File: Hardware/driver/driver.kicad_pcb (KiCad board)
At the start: 4 copper layers, 128.1 x 184.5 mm, 191 parts, among them J201 Conn_02x10_Odd_Even, J302 Würth 74651194R, J303 Würth 74651194R, J401 TBP02R2W-381-03BE, J402 Conn_01x02_Male, J501 Conn_Coaxial, J601 Screw_Terminal_01x02, K601 EC2-5TNU, M201 Fan_4pin, Q201 MMBT3904, Q202 PN2222A, Q301 IXTH80N075L2, Q302 IXTH80N075L2, Q601 MMBT3904, Q602 MMBT3904, U101 ICL7660, U102 DS2482-100, U103 PI4IOE5V9536, U201 AT24CS32-SSHM, U202 MIC5366-3.3YC5, U203 ADUM1250, U204 MCP1804x-C002xMB, U205 FODM217B, U206 EMC2101-R, U207 MCP1703AT-5002E/DB, U301 MCP3421A2T-ECH, U302 ADA4522-2, U303 DAC60501Z, U304 LM431SC, U305 MCP3421A3T-ECH, U306 ADA4522-2, U307 DAC60501Z, U308 LM431SC, U309 DS18B20, U310 DS18B20, U501 74LVC1G17, U502 FODM217B, U601 MCP3421A1T-ECH, U602 OPA277

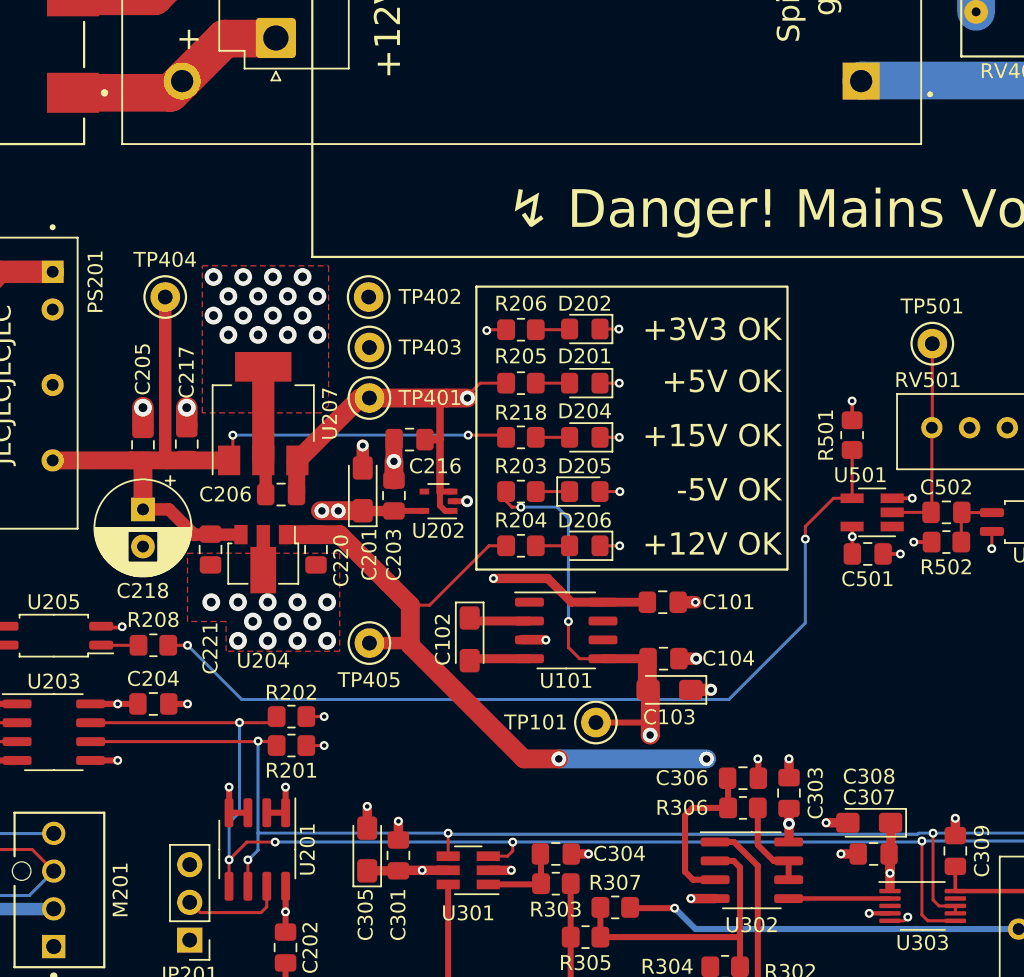
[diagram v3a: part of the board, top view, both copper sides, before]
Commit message: Fixed I2C bus reversal on driver
- Fixed an issue where SCL and SDA for the I2C bus were swapped beyond
  the interface sheet, meaning only the EEPROM is accessible over the
  bus. (This can probably be bodged relatively simply on a rev1 board on
  the bottom where the I2C bus runs)

- Manufacturability tweaks for TDK choke
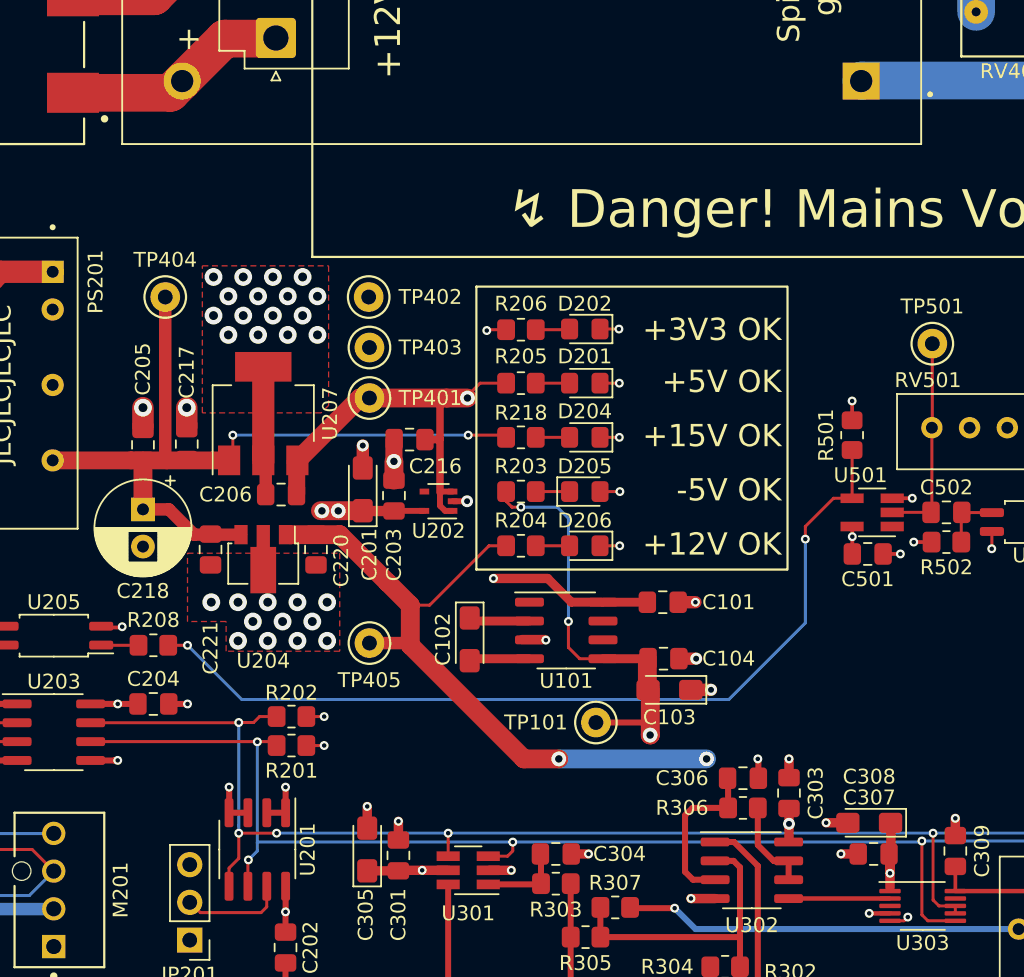
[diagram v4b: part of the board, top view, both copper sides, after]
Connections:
- R201 pad 1: /I2C_SDA -> /I2C_SCL
- R202 pad 1: /I2C_SCL -> /I2C_SDA
- U201 pad 5: /I2C_SCL -> /I2C_SDA
- U201 pad 6: /I2C_SDA -> /I2C_SCL
- U203 pad 6: /I2C_SDA -> /I2C_SCL
- U203 pad 7: /I2C_SCL -> /I2C_SDA
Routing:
- net /I2C_SCL: track 274.8 -> 271.7 mm, vias 10 -> 9
- net /I2C_SDA: track 266.2 -> 268.8 mm, vias 13 -> 14

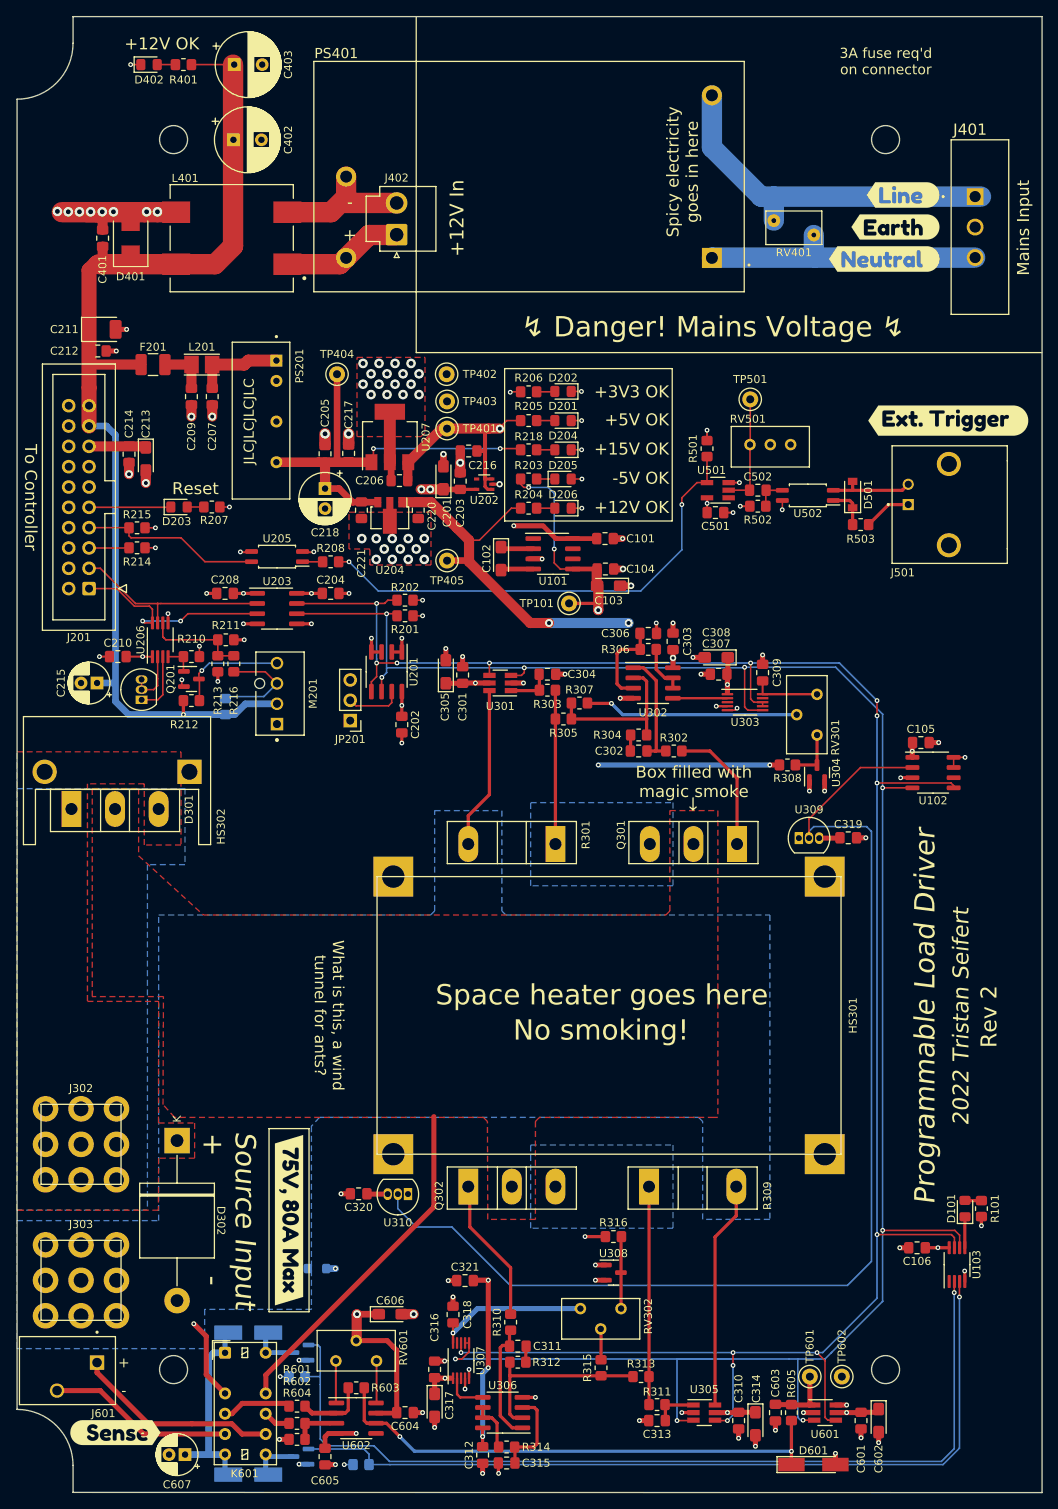
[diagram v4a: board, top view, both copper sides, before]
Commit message: Final bits of tweaks for rev2 analog board
- Fixed footprint of MMBT3904 transistors on driver and controller
  boards (it is SOT-323, not SC-70)

- A few more minor modifications to the layout of the analog driver
  board for rev2
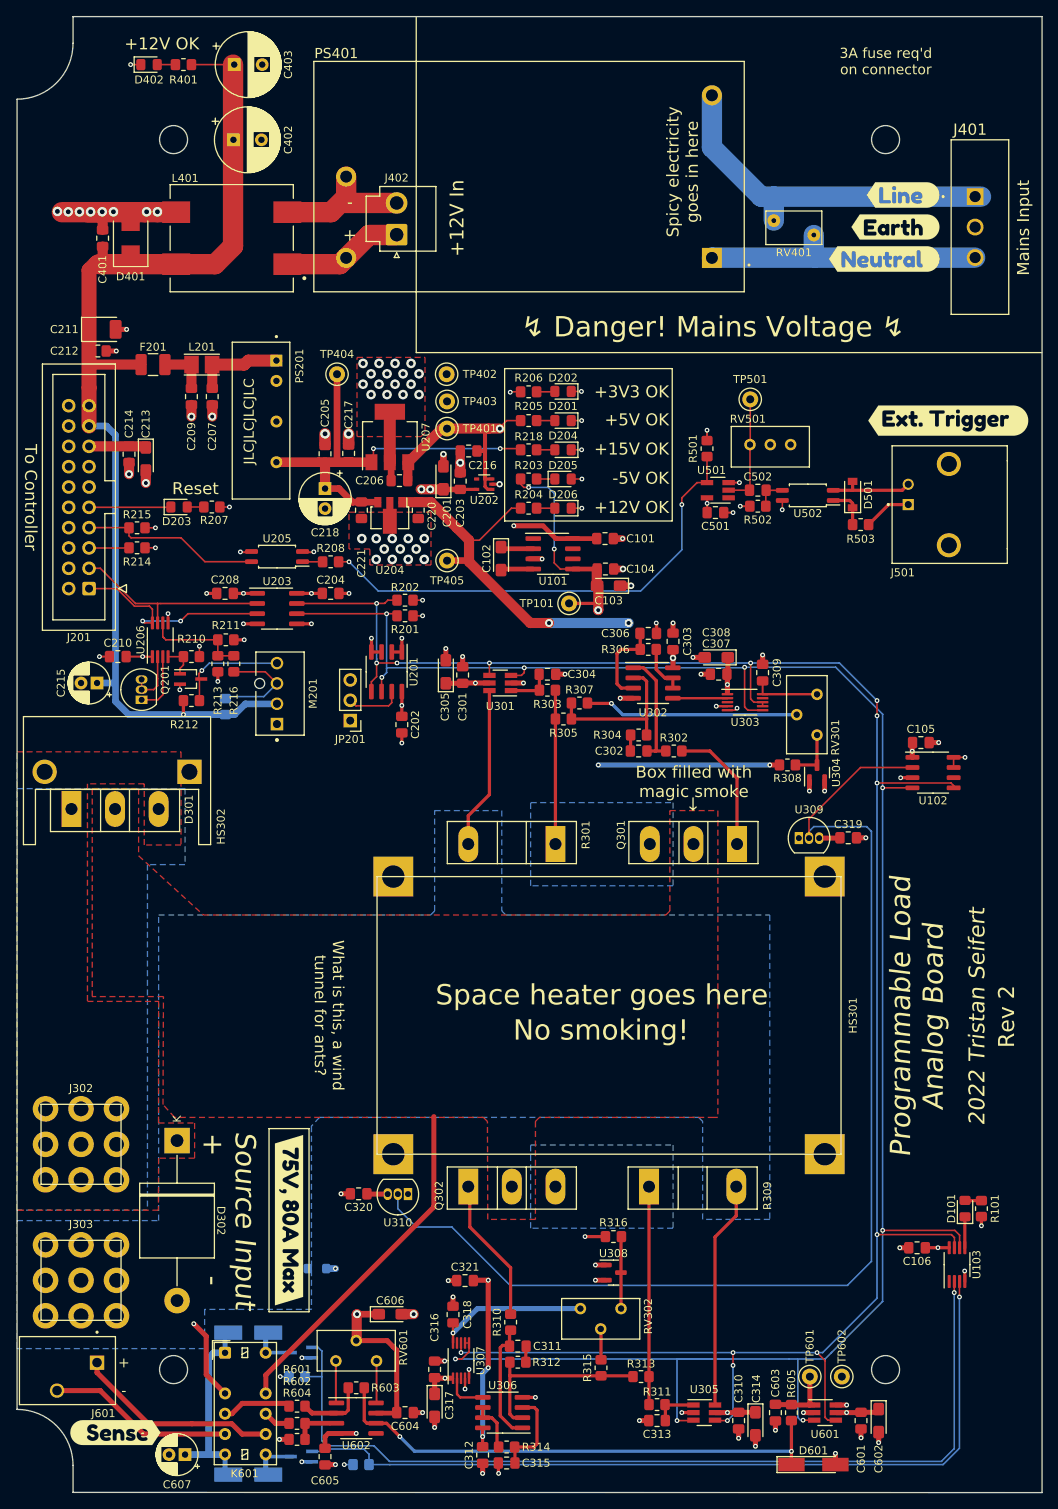
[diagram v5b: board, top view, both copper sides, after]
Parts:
- Q201, Q601, Q602: footprint Package_TO_SOT_SMD:SOT-23 -> Package_TO_SOT_SMD:SOT-323_SC-70_Handsoldering
- moved Q201 0.10 mm to (41.7, 102.8)
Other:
- board text added: "Programmable Load Analog Board"
- board text removed: "Programmable Load Driver"

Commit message: Fixed a few more footprints
- Made heatsink and connector mechanical/mounting pads NPTH instead of
  normal pads, so they're not tempted to be connected to regular signals
  on the board and get more keepout space
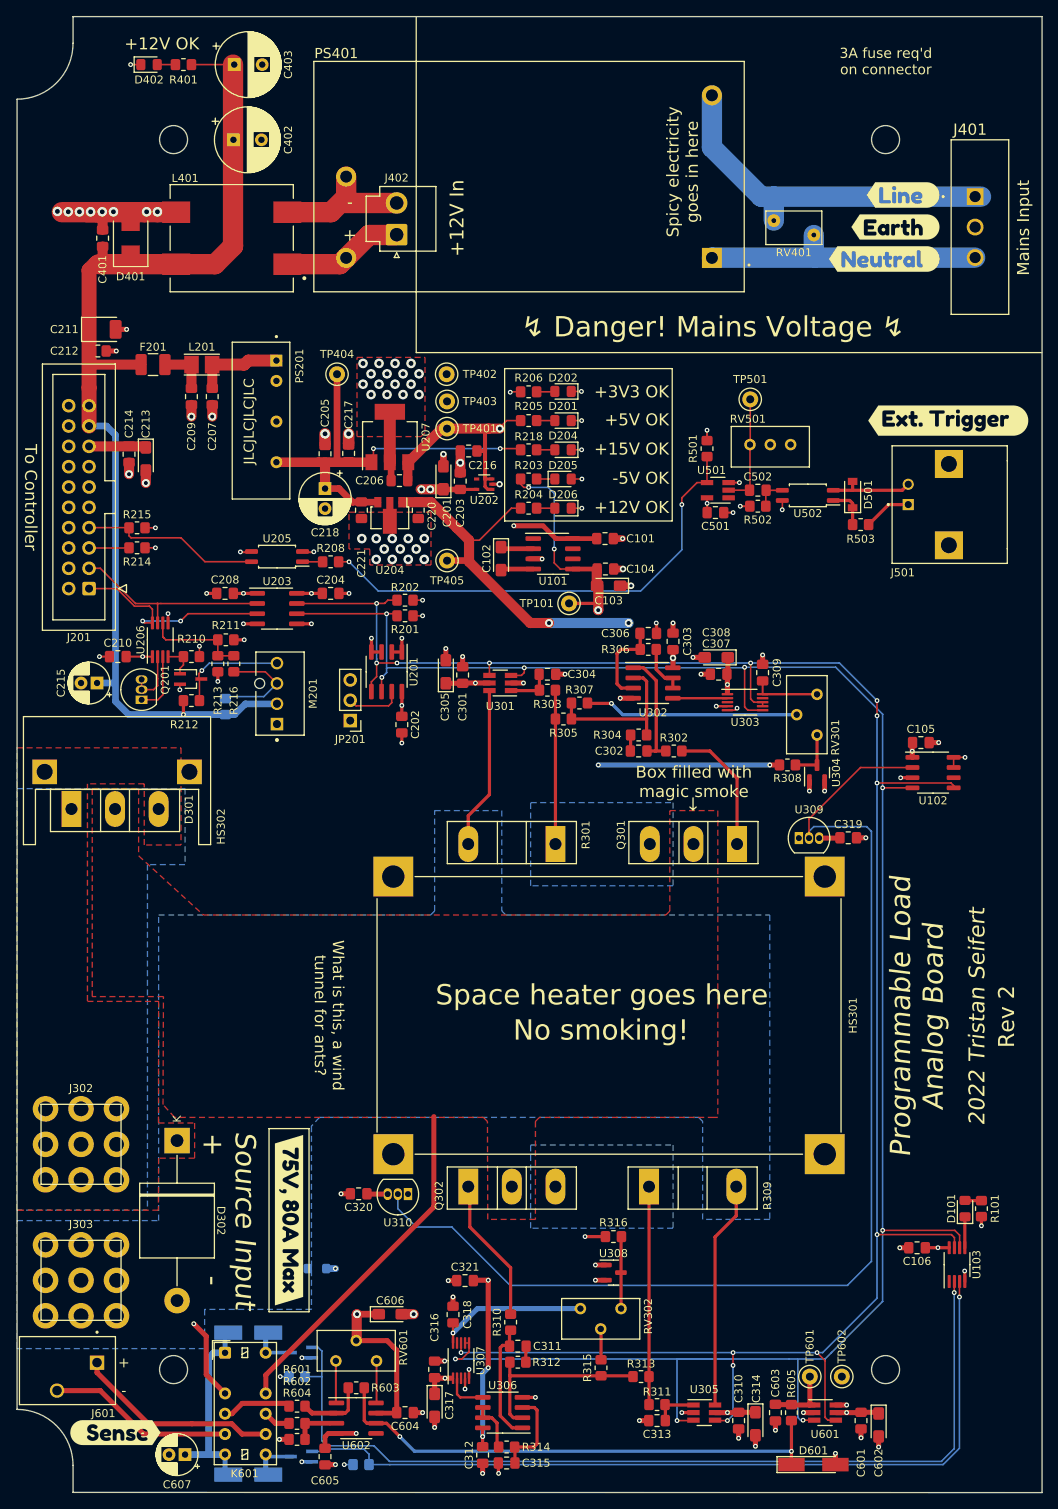
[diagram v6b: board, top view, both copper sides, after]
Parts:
- removed D203: Red, LED_SMD:LED_0805_2012Metric_Pad1.15x1.40mm_HandSolder
- removed R207: 1k, Resistor_SMD:R_0805_2012Metric_Pad1.20x1.40mm_HandSolder
- moved C602 0.55 mm to (127.7, 196.1)
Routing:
- net /External Interface/~{EXT_RESET}: track 10.6 -> 0.00 mm
- net Net-(D203-Pad2): track 2.08 -> 0.00 mm
- net +3V3A: track 19.8 -> 18.6 mm, vias 7 -> 6
- net +3V3: track 59.1 -> 58.6 mm
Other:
- board text removed: "Reset"
